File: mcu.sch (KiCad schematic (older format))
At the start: 18 parts, among them SW19 EVQQ2, SW8 EVQQ2, U9 STM32F405RGTx, Y1 8MHz

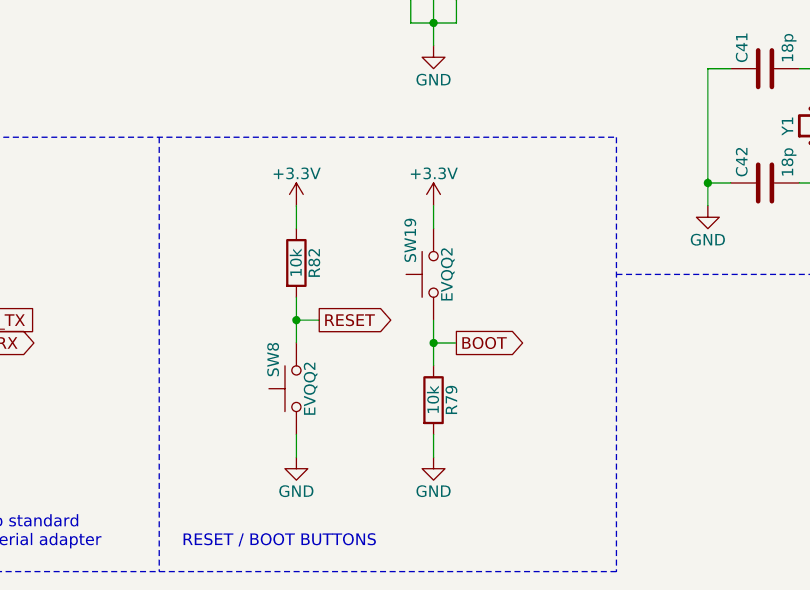
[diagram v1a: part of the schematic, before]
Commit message: add voltage supervisor, add leds to jacks, update footprints
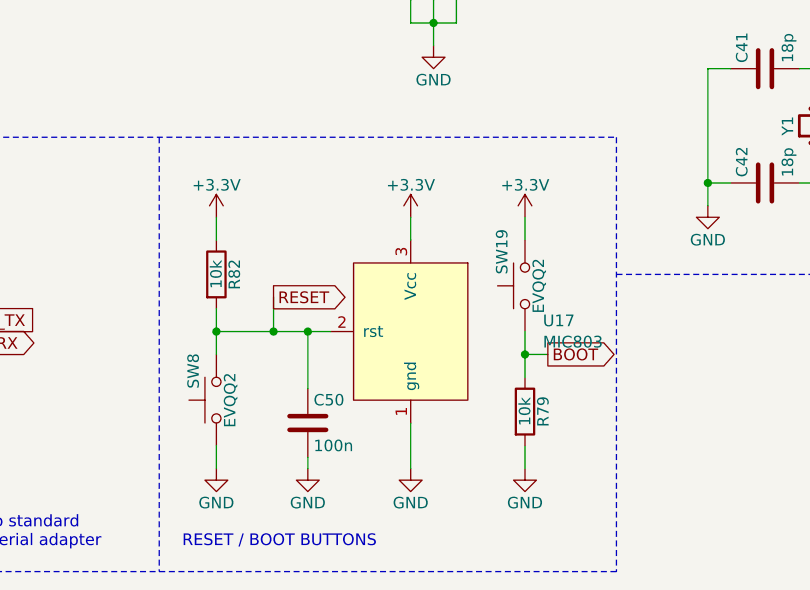
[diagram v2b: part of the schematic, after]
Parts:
- added C50: 100n, w_capacitor:C_0603, symbol Device:C
- added U17: MIC803, Package_TO_SOT_SMD:SOT-23, symbol w_power:MIC803
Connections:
- net +3V3: now also U17.3 (Vcc)
- net GND: now also C50.2, U17.1 (gnd)
- net RESET: now also C50.1, U17.2 (rst)
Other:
- moved on the sheet: R79, R82, SW19, SW8
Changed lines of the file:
@@
 EESchema Schematic File Version 4
-LIBS:sequencer-cache
-EELAYER 26 0
+EELAYER 30 0
 EELAYER END
 $Descr A4 11693 8268
@@
 L Switch:SW_Push SW19
 U 1 1 59DD439D
-P 5800 6400
-F 0 "SW19" H 5850 6500 50  0000 L CNN
-F 1 "EVQQ2" H 5800 6340 50  0000 C CNN
-F 2 "Button_Switch_SMD:SW_SPST_EVQQ2" H 5800 6600 50  0001 C CNN
-F 3 "http://datasheet.octopart.com/EVQ-Q2K01W-Panasonic-datasheet-13267673.pdf" H 5800 6600 50  0001 C CNN
-F 4 "Panasonic" H 5850 6600 50  0001 C CNN "MFN"
-F 5 "EVQ-Q2K01W" H 5850 6600 50  0001 C CNN "MFP"
-	1    5800 6400
+P 6200 6450
+F 0 "SW19" H 6250 6550 50  0000 L CNN
+F 1 "EVQQ2" H 6200 6390 50  0000 C CNN
+F 2 "Button_Switch_SMD:SW_SPST_EVQQ2" H 6200 6650 50  0001 C CNN
+F 3 "http://datasheet.octopart.com/EVQ-Q2K01W-Panasonic-datasheet-13267673.pdf" H 6200 6650 50  0001 C CNN
+F 4 "Panasonic" H 6250 6650 50  0001 C CNN "MFN"
+F 5 "EVQ-Q2K01W" H 6250 6650 50  0001 C CNN "MFP"
+	1    6200 6450
 	0    -1   -1   0
 $EndComp
@@
 L Switch:SW_Push SW8
 U 1 1 59DD44E7
-P 5200 6900
-F 0 "SW8" H 5250 7000 50  0000 L CNN
-F 1 "EVQQ2" H 5200 6840 50  0000 C CNN
-F 2 "Button_Switch_SMD:SW_SPST_EVQQ2" H 5200 7100 50  0001 C CNN
-F 3 "http://datasheet.octopart.com/EVQ-Q2K01W-Panasonic-datasheet-13267673.pdf" H 5200 7100 50  0001 C CNN
-F 4 "Panasonic" H 5250 7100 50  0001 C CNN "MFN"
-F 5 "EVQ-Q2K01W" H 5250 7100 50  0001 C CNN "MFP"
-	1    5200 6900
+P 4850 6950
+F 0 "SW8" H 4900 7050 50  0000 L CNN
+F 1 "EVQQ2" H 4850 6890 50  0000 C CNN
+F 2 "Button_Switch_SMD:SW_SPST_EVQQ2" H 4850 7150 50  0001 C CNN
+F 3 "http://datasheet.octopart.com/EVQ-Q2K01W-Panasonic-datasheet-13267673.pdf" H 4850 7150 50  0001 C CNN
+F 4 "Panasonic" H 4900 7150 50  0001 C CNN "MFN"
+F 5 "EVQ-Q2K01W" H 4900 7150 50  0001 C CNN "MFP"
+	1    4850 6950
 	0    -1   -1   0
 $EndComp
@@
 L Device:R R82
 U 1 1 59DD490D
-P 5200 6350
-F 0 "R82" V 5280 6350 50  0000 C CNN
-F 1 "10k" V 5200 6350 50  0000 C CNN
-F 2 "w_resistor:R_0603" V 5130 6350 50  0001 C CNN
-F 3 "http://datasheet.octopart.com/ERJ-3EKF1002V-Panasonic-datasheet-13266541.pdf" H 5200 6350 50  0001 C CNN
-F 4 "Panasonic" H 5280 6450 50  0001 C CNN "MFN"
-F 5 "ERJ-3EKF1002V" H 5280 6450 50  0001 C CNN "MFP"
-F 6 "0603" H 5280 6450 50  0001 C CNN "Package"
-	1    5200 6350
+P 4850 6400
+F 0 "R82" V 4930 6400 50  0000 C CNN
+F 1 "10k" V 4850 6400 50  0000 C CNN
+F 2 "w_resistor:R_0603" V 4780 6400 50  0001 C CNN
+F 3 "http://datasheet.octopart.com/ERJ-3EKF1002V-Panasonic-datasheet-13266541.pdf" H 4850 6400 50  0001 C CNN
+F 4 "Panasonic" H 4930 6500 50  0001 C CNN "MFN"
+F 5 "ERJ-3EKF1002V" H 4930 6500 50  0001 C CNN "MFP"
+F 6 "0603" H 4930 6500 50  0001 C CNN "Package"
+	1    4850 6400
 	1    0    0    -1
 $EndComp
@@
 L Device:R R79
 U 1 1 59DD4953
-P 5800 6950
-F 0 "R79" V 5880 6950 50  0000 C CNN
-F 1 "10k" V 5800 6950 50  0000 C CNN
-F 2 "w_resistor:R_0603" V 5730 6950 50  0001 C CNN
-F 3 "http://datasheet.octopart.com/ERJ-3EKF1002V-Panasonic-datasheet-13266541.pdf" H 5800 6950 50  0001 C CNN
-F 4 "Panasonic" H 5880 7050 50  0001 C CNN "MFN"
-F 5 "ERJ-3EKF1002V" H 5880 7050 50  0001 C CNN "MFP"
-F 6 "0603" H 5880 7050 50  0001 C CNN "Package"
-	1    5800 6950
+P 6200 7000
+F 0 "R79" V 6280 7000 50  0000 C CNN
+F 1 "10k" V 6200 7000 50  0000 C CNN
+F 2 "w_resistor:R_0603" V 6130 7000 50  0001 C CNN
+F 3 "http://datasheet.octopart.com/ERJ-3EKF1002V-Panasonic-datasheet-13266541.pdf" H 6200 7000 50  0001 C CNN
+F 4 "Panasonic" H 6280 7100 50  0001 C CNN "MFN"
+F 5 "ERJ-3EKF1002V" H 6280 7100 50  0001 C CNN "MFP"
+F 6 "0603" H 6280 7100 50  0001 C CNN "Package"
+	1    6200 7000
 	1    0    0    -1
 $EndComp
@@
 L power:+3.3V #PWR063
 U 1 1 59DD49A9
-P 5200 6100
-F 0 "#PWR063" H 5200 5950 50  0001 C CNN
-F 1 "+3.3V" H 5200 6240 50  0000 C CNN
-F 2 "" H 5200 6100 50  0001 C CNN
-F 3 "" H 5200 6100 50  0001 C CNN
-	1    5200 6100
+P 4850 6150
+F 0 "#PWR063" H 4850 6000 50  0001 C CNN
+F 1 "+3.3V" H 4850 6290 50  0000 C CNN
+F 2 "" H 4850 6150 50  0001 C CNN
+F 3 "" H 4850 6150 50  0001 C CNN
+	1    4850 6150
 	1    0    0    -1
 $EndComp
@@
 L power:+3.3V #PWR064
 U 1 1 59DD49E1
-P 5800 6100
-F 0 "#PWR064" H 5800 5950 50  0001 C CNN
-F 1 "+3.3V" H 5800 6240 50  0000 C CNN
-F 2 "" H 5800 6100 50  0001 C CNN
-F 3 "" H 5800 6100 50  0001 C CNN
-	1    5800 6100
+P 6200 6150
+F 0 "#PWR064" H 6200 6000 50  0001 C CNN
+F 1 "+3.3V" H 6200 6290 50  0000 C CNN
+F 2 "" H 6200 6150 50  0001 C CNN
+F 3 "" H 6200 6150 50  0001 C CNN
+	1    6200 6150
 	1    0    0    -1
 $EndComp
@@
 L power:GND #PWR065
 U 1 1 59DD4A83
-P 5200 7200
-F 0 "#PWR065" H 5200 6950 50  0001 C CNN
-F 1 "GND" H 5200 7050 50  0000 C CNN
-F 2 "" H 5200 7200 50  0001 C CNN
-F 3 "" H 5200 7200 50  0001 C CNN
-	1    5200 7200
+P 4850 7250
+F 0 "#PWR065" H 4850 7000 50  0001 C CNN
+F 1 "GND" H 4850 7100 50  0000 C CNN
+F 2 "" H 4850 7250 50  0001 C CNN
+F 3 "" H 4850 7250 50  0001 C CNN
+	1    4850 7250
 	1    0    0    -1
 $EndComp
@@
 L power:GND #PWR066
 U 1 1 59DD4ABB
-P 5800 7200
-F 0 "#PWR066" H 5800 6950 50  0001 C CNN
-F 1 "GND" H 5800 7050 50  0000 C CNN
-F 2 "" H 5800 7200 50  0001 C CNN
-F 3 "" H 5800 7200 50  0001 C CNN
-	1    5800 7200
+P 6200 7250
+F 0 "#PWR066" H 6200 7000 50  0001 C CNN
+F 1 "GND" H 6200 7100 50  0000 C CNN
+F 2 "" H 6200 7250 50  0001 C CNN
+F 3 "" H 6200 7250 50  0001 C CNN
+	1    6200 7250
 	1    0    0    -1
 $EndComp
@@
 Text GLabel 10200 3600 2    51   Input ~ 0
 SYS_JTDO
-Text GLabel 5300 6600 2    51   Output ~ 0
+Text GLabel 5100 6500 2    51   Output ~ 0
 RESET
-Text GLabel 5900 6700 2    51   Output ~ 0
+Text GLabel 6300 6750 2    51   Output ~ 0
 BOOT
 Text GLabel 1400 2800 0    51   Input ~ 0
@@
 	800  2150 800  2250
 Wire Wire Line
-	5200 6100 5200 6200
-Wire Wire Line
-	5200 6500 5200 6600
-Wire Wire Line
-	5200 6600 5300 6600
-Wire Wire Line
-	5200 7100 5200 7200
-Wire Wire Line
-	5800 6100 5800 6200
-Wire Wire Line
-	5800 6600 5800 6700
-Wire Wire Line
-	5800 6700 5900 6700
-Wire Wire Line
-	5800 7100 5800 7200
+	4850 6150 4850 6250
+Wire Wire Line
+	4850 6550 4850 6650
+Wire Wire Line
+	4850 7150 4850 7250
+Wire Wire Line
+	6200 6150 6200 6250
+Wire Wire Line
+	6200 6650 6200 6750
+Wire Wire Line
+	6200 6750 6300 6750
+Wire Wire Line
+	6200 7150 6200 7250
 Wire Wire Line
 	1400 2800 1500 2800
@@
 	900  2150 900  2250
 Wire Wire Line
-	5200 6600 5200 6700
-Wire Wire Line
-	5800 6700 5800 6800
+	4850 6650 4850 6750
+Wire Wire Line
+	6200 6750 6200 6850
 Wire Wire Line
 	8600 5500 8900 5500
@@
 Connection ~ 7500 6000
 Connection ~ 900  2150
-Connection ~ 5200 6600
-Connection ~ 5800 6700
+Connection ~ 4850 6650
+Connection ~ 6200 6750
 Connection ~ 8600 5500
 Connection ~ 8900 5500
@@
 NoConn ~ 1500 3300
 NoConn ~ 1500 3400
+$Comp
+L w_power:MIC803 U17
+U 1 1 5EF4CA8D
+P 5700 6600
+F 0 "U17" H 5122 6597 51  0000 R CNN
+F 1 "MIC803" H 5122 6504 51  0000 R CNN
+F 2 "Package_TO_SOT_SMD:SOT-23" H 5500 6900 51  0001 C CNN
+F 3 "" H 5500 6900 51  0001 C CNN
+	1    5700 6600
+	-1   0    0    -1
+$EndComp
+$Comp
+L power:+3.3V #PWR0126
+U 1 1 5EF4E0F9
+P 5700 6150
+F 0 "#PWR0126" H 5700 6000 50  0001 C CNN
+F 1 "+3.3V" H 5700 6290 50  0000 C CNN
+F 2 "" H 5700 6150 50  0001 C CNN
+F 3 "" H 5700 6150 50  0001 C CNN
+	1    5700 6150
+	1    0    0    -1
+$EndComp
+$Comp
+L power:GND #PWR0127
+U 1 1 5EF4E7C6
+P 5700 7250
+F 0 "#PWR0127" H 5700 7000 50  0001 C CNN
+F 1 "GND" H 5700 7100 50  0000 C CNN
+F 2 "" H 5700 7250 50  0001 C CNN
+F 3 "" H 5700 7250 50  0001 C CNN
+	1    5700 7250
+	1    0    0    -1
+$EndComp
+$Comp
+L Device:C C50
+U 1 1 5EF4EC86
+P 5250 7050
+F 0 "C50" H 5275 7150 50  0000 L CNN
+F 1 "100n" H 5275 6950 50  0000 L CNN
+F 2 "w_capacitor:C_0603" H 5288 6900 50  0001 C CNN
+F 3 "http://datasheet.octopart.com/GRM1885C1H180JA01J-Murata-datasheet-66077082.pdf" H 5250 7050 50  0001 C CNN
+F 4 "Murata" H 5275 7250 50  0001 C CNN "MFN"
+F 5 "GRM1885C1H180JA01J" H 5275 7250 50  0001 C CNN "MFP"
+F 6 "0603" H 5275 7250 50  0001 C CNN "Package"
+	1    5250 7050
+	1    0    0    -1
+$EndComp
+$Comp
+L power:GND #PWR0128
+U 1 1 5EF4F690
+P 5250 7250
+F 0 "#PWR0128" H 5250 7000 50  0001 C CNN
+F 1 "GND" H 5250 7100 50  0000 C CNN
+F 2 "" H 5250 7250 50  0001 C CNN
+F 3 "" H 5250 7250 50  0001 C CNN
+	1    5250 7250
+	1    0    0    -1
+$EndComp
+Wire Wire Line
+	5700 7250 5700 7050
+Wire Wire Line
+	5700 6250 5700 6150
+Wire Wire Line
+	5250 7200 5250 7250
+Wire Wire Line
+	5250 6900 5250 6650
+Wire Wire Line
+	5250 6650 5350 6650
+Wire Wire Line
+	4850 6650 5100 6650
+Connection ~ 5250 6650
+Wire Wire Line
+	5100 6500 5100 6650
+Connection ~ 5100 6650
+Wire Wire Line
+	5100 6650 5250 6650
 $EndSCHEMATC

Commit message: small changes
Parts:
- C18, C23: footprint w_capacitor:C_0805 -> w_capacitor:C_0603
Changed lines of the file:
@@
 F 0 "C23" H 1175 2150 50  0000 L CNN
 F 1 "2.2u" H 1175 1950 50  0000 L CNN
-F 2 "w_capacitor:C_0805" H 1188 1900 50  0001 C CNN
+F 2 "w_capacitor:C_0603" H 1188 1900 50  0001 C CNN
 F 3 "http://datasheet.octopart.com/C2012X5R1A225K085AA-TDK-datasheet-41194876.pdf" H 1150 2050 50  0001 C CNN
 F 4 "TDK" H 1175 2250 50  0001 C CNN "MFN"
@@
 F 0 "C18" H 1175 2350 50  0000 L CNN
 F 1 "2.2u" H 1175 2150 50  0000 L CNN
-F 2 "w_capacitor:C_0805" H 1188 2100 50  0001 C CNN
+F 2 "w_capacitor:C_0603" H 1188 2100 50  0001 C CNN
 F 3 "http://datasheet.octopart.com/C2012X5R1A225K085AA-TDK-datasheet-41194876.pdf" H 1150 2250 50  0001 C CNN
 F 4 "TDK" H 1175 2450 50  0001 C CNN "MFN"
